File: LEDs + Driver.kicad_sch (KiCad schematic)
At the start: 1 part, among them U1 LP5860

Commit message: Progress commit. Added MCU + IMU.
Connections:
- net Bottom LEDs/SW5: now reaches U1.15 (SW5)
- net Bottom LEDs/SW6: now reaches U1.17 (SW6)
- net Bottom LEDs/SW7: now reaches U1.18 (SW7)
- net Bottom LEDs/SW8: now reaches U1.19 (SW8)
- net Bottom LEDs/SW9: now reaches U1.20 (SW9)
- net GND: now reaches U1.31 (AGND)
- net GND: now also U1.41 (GND)
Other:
- sheet Bottom LEDs ports: added SW5, SW6, SW7, SW8, SW9; removed none

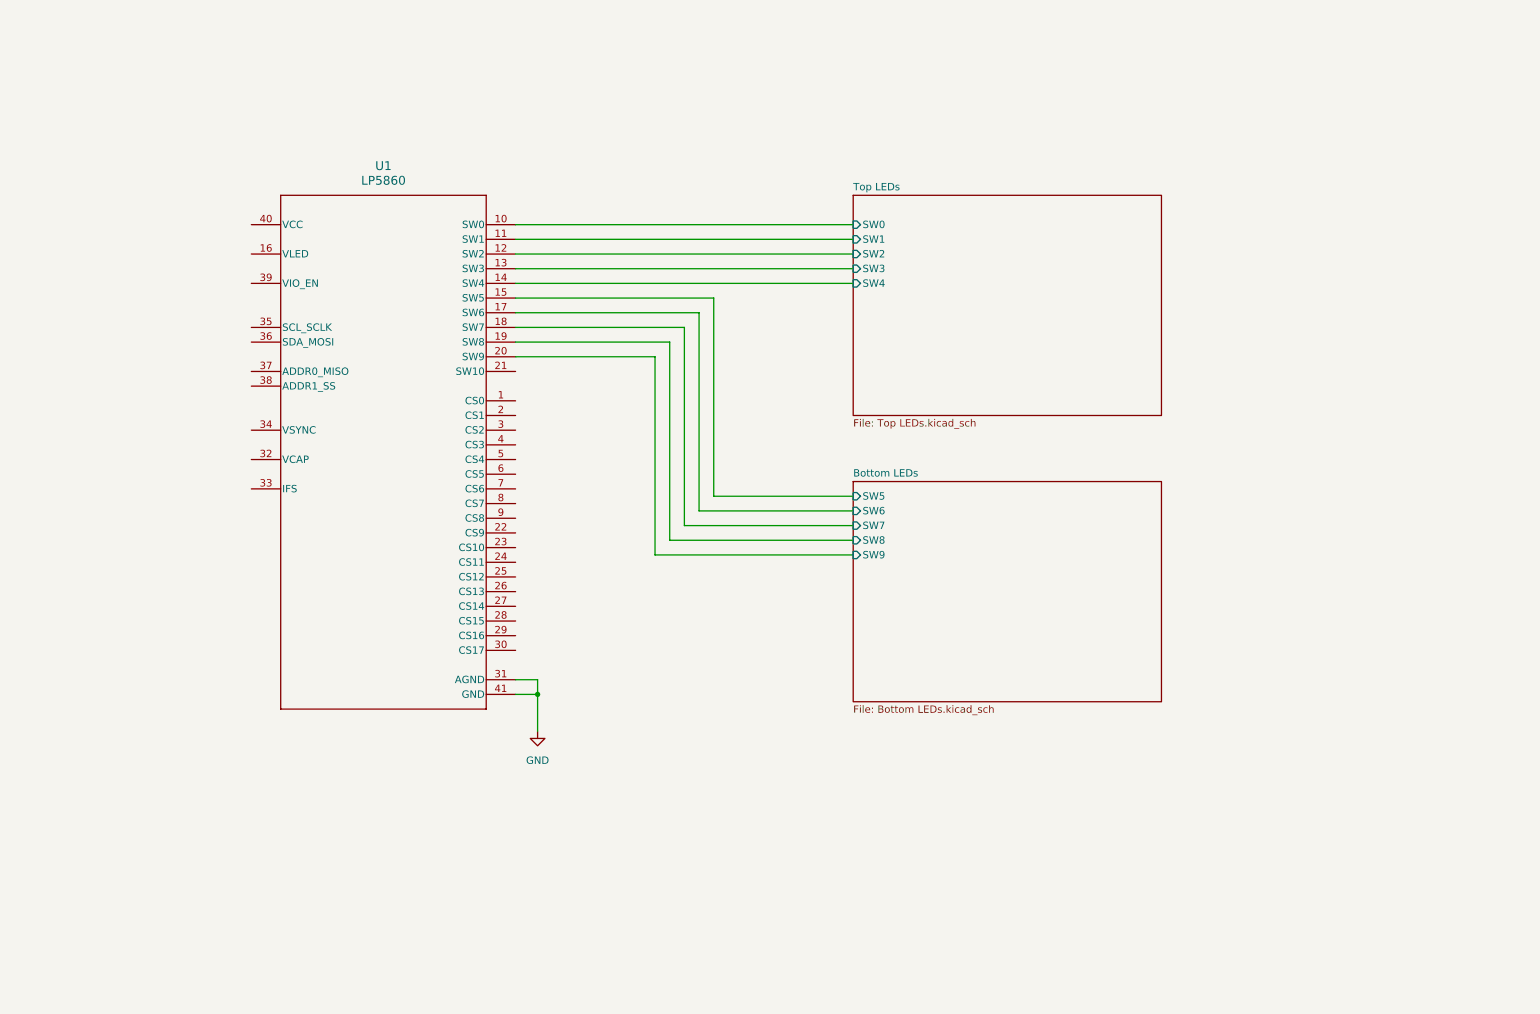
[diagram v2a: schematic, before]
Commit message: Initial complete implementation of LEDS.
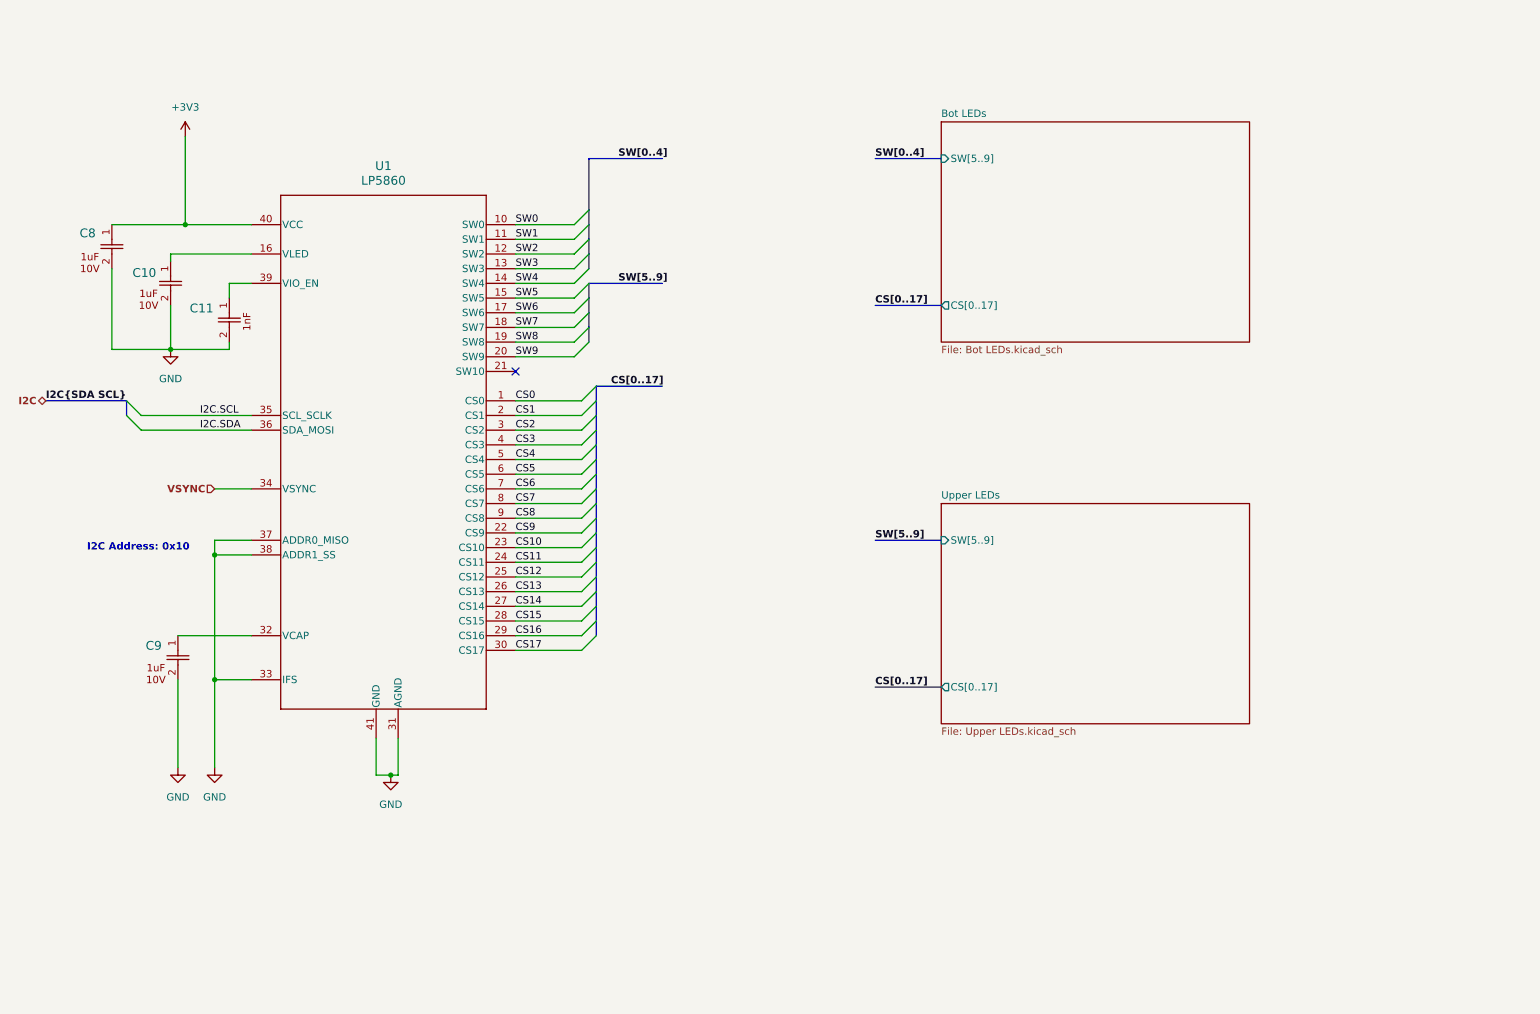
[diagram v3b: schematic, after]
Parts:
- added C10, C8, C9: GRM155Z71A105KE01D, Hourglass_footprint_library:CAP_GRM155Z_MUR, symbol Hourglass_symbol_library:GRM155Z71A105KE01D
- added C11: SH05B102K251DC, Hourglass_footprint_library:CAP_CL21_SAM, symbol Hourglass_symbol_library:SH05B102K251DC
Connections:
- net GND: now also U1.33 (IFS), U1.37 (ADDR0_MISO), U1.38 (ADDR1_SS), C10.2, C11.2, C8.2, C9.2
- net CS0: now reaches U1.1 (CS0)
- net at U1.16 (VLED): now also C10.1
- net CS1: now reaches U1.2 (CS1)
- net CS9: now reaches U1.22 (CS9)
- net CS10: now reaches U1.23 (CS10)
- net CS11: now reaches U1.24 (CS11)
- net CS12: now reaches U1.25 (CS12)
- net CS13: now reaches U1.26 (CS13)
- net CS14: now reaches U1.27 (CS14)
- net CS15: now reaches U1.28 (CS15)
- net CS16: now reaches U1.29 (CS16)
- net CS2: now reaches U1.3 (CS2)
- net CS17: now reaches U1.30 (CS17)
- net at U1.32 (VCAP): now also C9.1
- net VSYNC: now reaches U1.34 (VSYNC)
- net I2C.SCL: now reaches U1.35 (SCL_SCLK)
- net I2C.SDA: now reaches U1.36 (SDA_MOSI)
- net at U1.39 (VIO_EN): now also C11.1
- net CS3: now reaches U1.4 (CS3)
- net +3V3: now reaches U1.40 (VCC)
- net +3V3: now also C8.1
- net CS4: now reaches U1.5 (CS4)
- net CS5: now reaches U1.6 (CS5)
- net CS6: now reaches U1.7 (CS6)
- net CS7: now reaches U1.8 (CS7)
- net CS8: now reaches U1.9 (CS8)
- net Bottom LEDs/SW5 renamed SW5
- net Bottom LEDs/SW6 renamed SW6
- net Bottom LEDs/SW7 renamed SW7
- net Bottom LEDs/SW8 renamed SW8
- net Bottom LEDs/SW9 renamed SW9
- net Bot LEDs/SW0 renamed SW0
- net Bot LEDs/SW1 renamed SW1
- net Bot LEDs/SW2 renamed SW2
- net Bot LEDs/SW3 renamed SW3
- net Bot LEDs/SW4 renamed SW4
- no-connect marks 0 -> 1
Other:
- sheet Top LEDs renamed Bot LEDs
- removed sheet Bottom LEDs
- added sheet Upper LEDs (Upper LEDs.kicad_sch)
- sheet Bot LEDs: file Top LEDs.kicad_sch -> Bot LEDs.kicad_sch
- sheet Bot LEDs ports: added CS[0..17], SW[5..9]; removed SW0, SW1, SW2, SW3, SW4
- note added: "I2C Address: 0x10"
- moved on the sheet: U1

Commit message: Completed schematic for MCU section
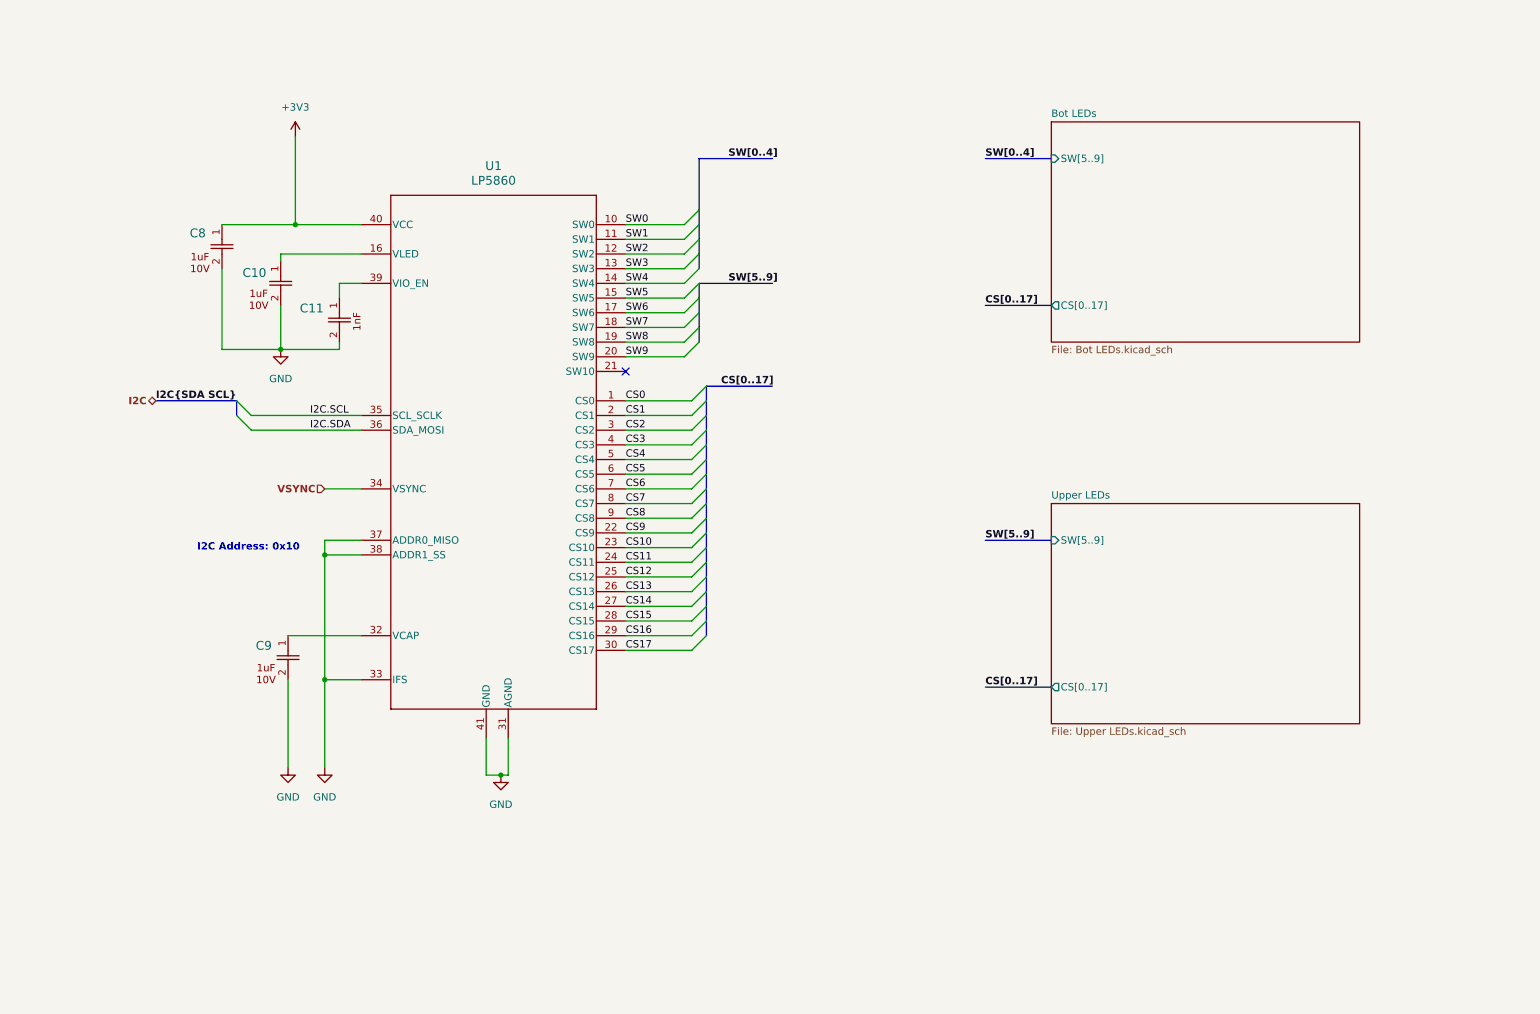
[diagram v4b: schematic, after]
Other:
- moved on the sheet: C10, C11, C8, C9, U1

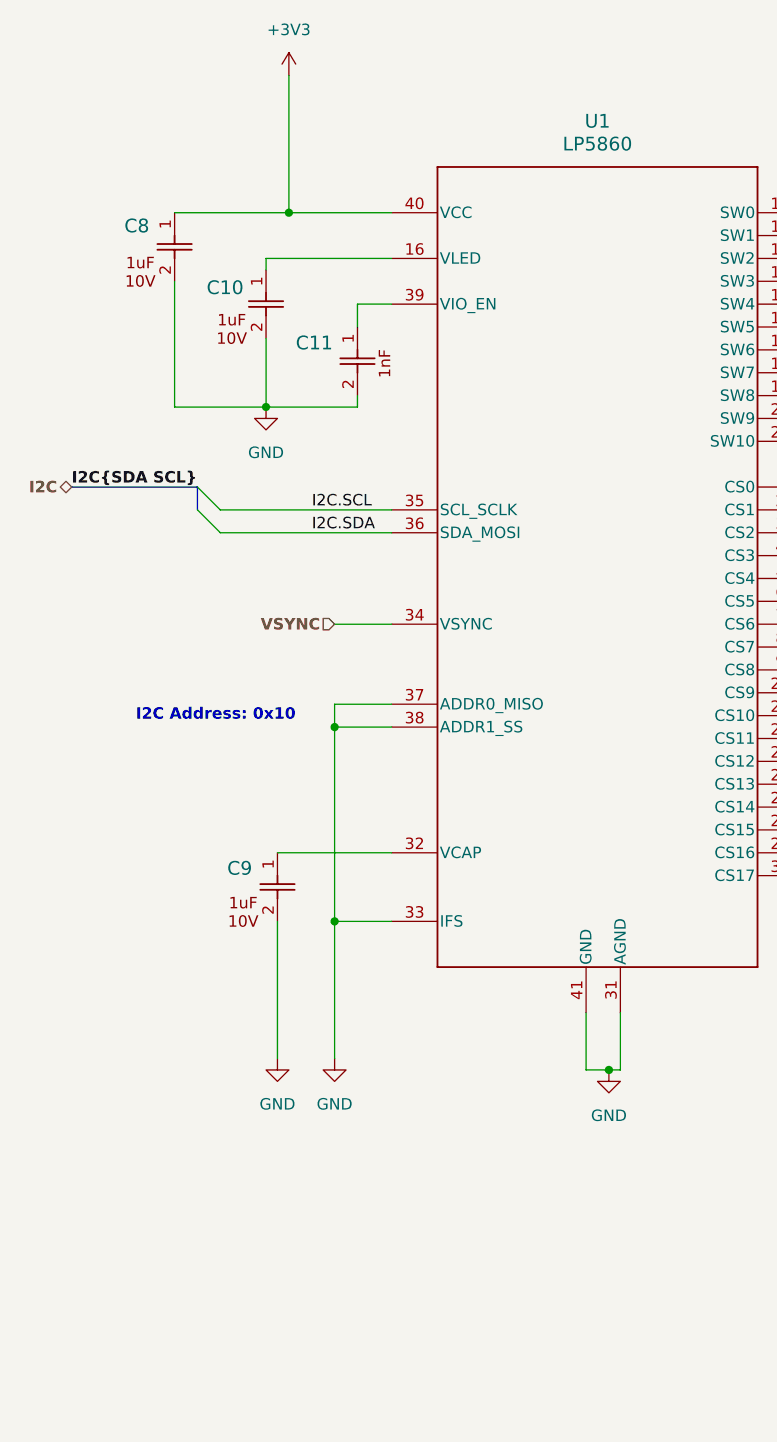
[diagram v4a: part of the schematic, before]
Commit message: First complete schematic with TPs.
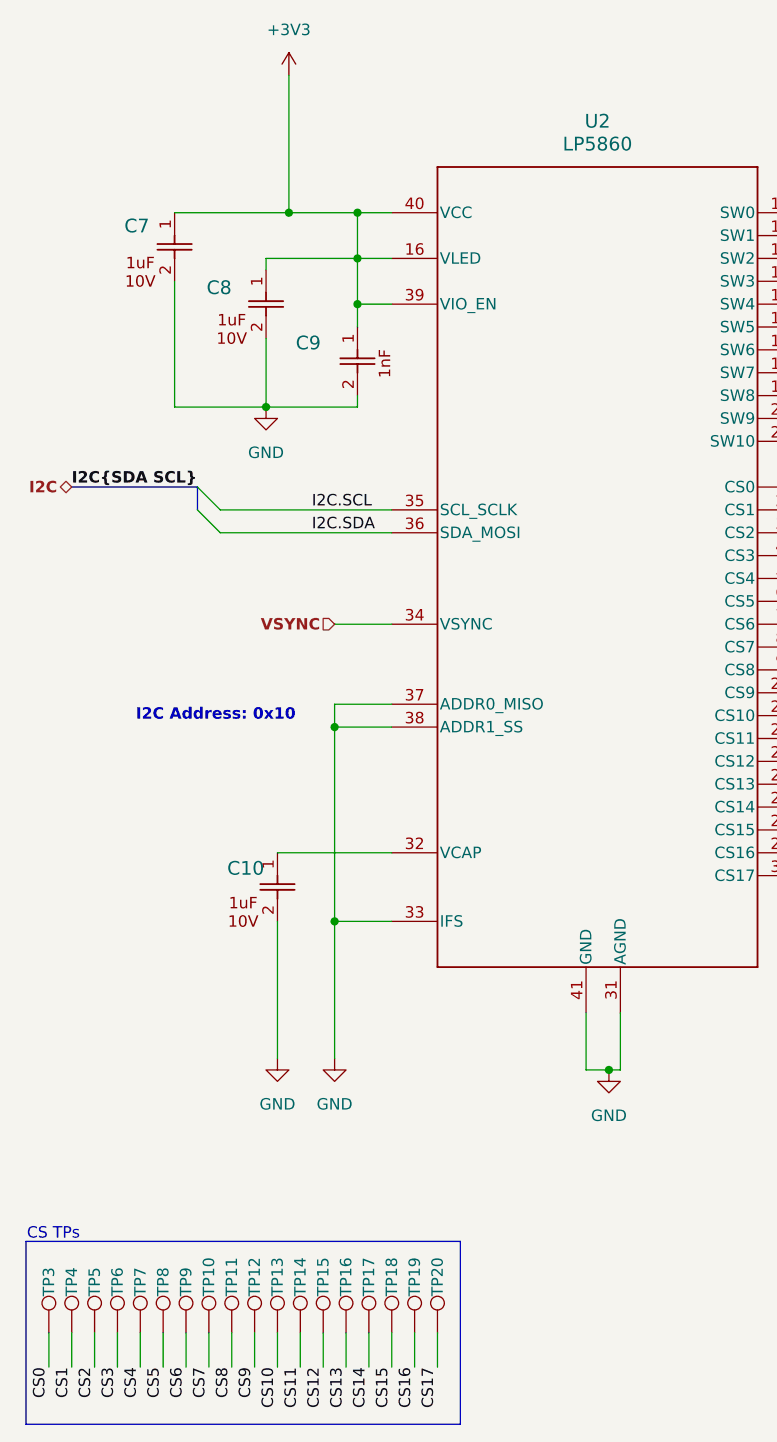
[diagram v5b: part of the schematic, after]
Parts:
- added TP10, TP11, TP12, TP13, TP14, TP15, TP16, TP17, TP18, TP19, TP20, TP3, TP4, TP5, TP6, TP7, TP8, TP9: TestPoint, TestPoint:TestPoint_Pad_D1.0mm, symbol Connector:TestPoint
- renumbered C9 to C10, C8 to C7, C10 to C8, C11 to C9, U1 to U2
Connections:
- net +3V3: now also C8.1, C9.1, U2.16 (VLED), U2.39 (VIO_EN)
- net CS0: now also TP3.1
- net CS1: now also TP4.1
- net CS10: now also TP13.1
- net CS11: now also TP14.1
- net CS12: now also TP15.1
- net CS13: now also TP16.1
- net CS14: now also TP17.1
- net CS15: now also TP18.1
- net CS16: now also TP19.1
- net CS17: now also TP20.1
- net CS2: now also TP5.1
- net CS3: now also TP6.1
- net CS4: now also TP7.1
- net CS5: now also TP8.1
- net CS6: now also TP9.1
- net CS7: now also TP10.1
- net CS8: now also TP11.1
- net CS9: now also TP12.1
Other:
- note added: "CS TPs"

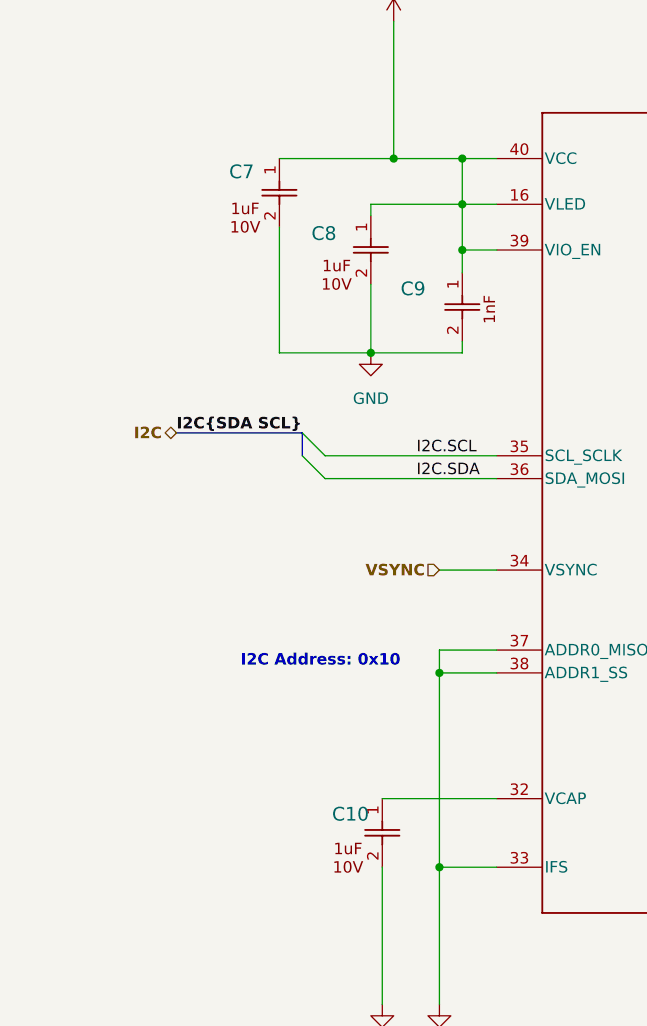
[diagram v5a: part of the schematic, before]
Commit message: Addressed DRC warnings and errors.
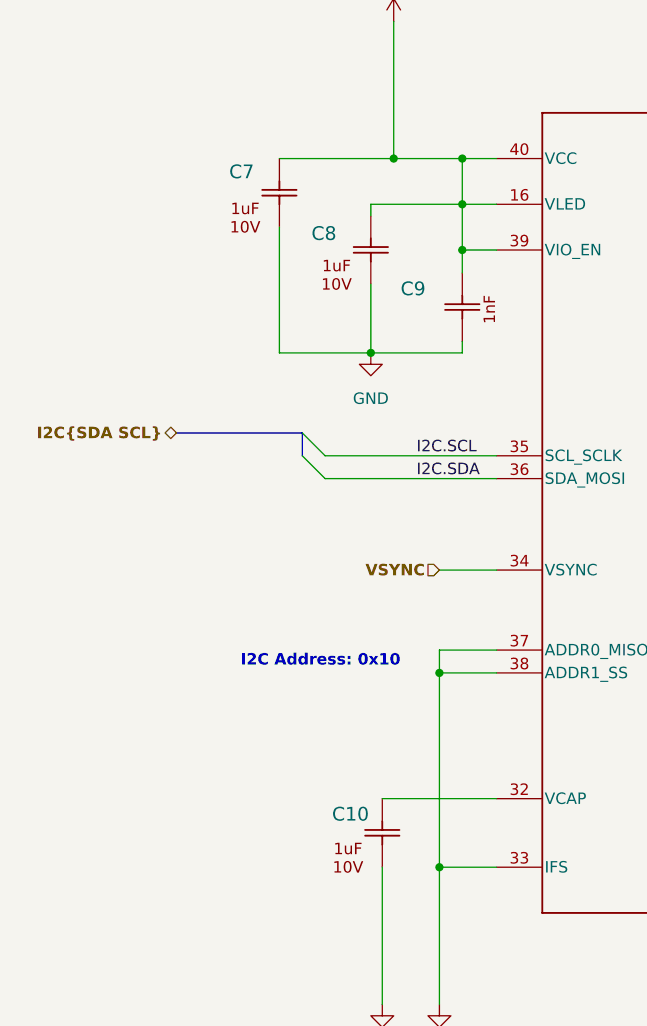
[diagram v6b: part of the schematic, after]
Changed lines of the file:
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@@
-		)
-	)
-	(label "I2C{SDA SCL}"
-		(at 40.64 83.82 0)
-		(effects
-			(font
-				(size 1.27 1.27)
-				(thickness 0.254)
-				(bold yes)
-			)
-			(justify left bottom)
 		)
 	)
@@
 		)
 	)
-	(hierarchical_label "I2C"
+	(hierarchical_label "I2C{SDA SCL}"
 		(shape bidirectional)
 		(at 40.64 83.82 180)
@@
 		(dnp no)
 		(fields_autoplaced yes)
-		(property "Reference" "#PWR015"
+		(property "Reference" "#PWR15"
 			(at 100.33 154.94 0)
 			(effects
@@
 			(project ""
 				(path "/a75630d2-15a7-42bc-8ce0-7846cbd1da6b/9c708963-e8cc-42a5-9c83-1e957695e1ca"
-					(reference "#PWR015")
+					(reference "#PWR15")
 					(unit 1)
 				)
@@
 		(dnp no)
 		(fields_autoplaced yes)
-		(property "Reference" "#PWR013"
+		(property "Reference" "#PWR13"
 			(at 63.5 153.67 0)
 			(effects
@@
 			(project "Hourglass_PCBA"
 				(path "/a75630d2-15a7-42bc-8ce0-7846cbd1da6b/9c708963-e8cc-42a5-9c83-1e957695e1ca"
-					(reference "#PWR013")
+					(reference "#PWR13")
 					(unit 1)
 				)
@@
 		(on_board yes)
 		(dnp no)
-		(property "Reference" "#PWR011"
+		(property "Reference" "#PWR11"
 			(at 64.77 41.91 0)
 			(effects
@@
 			(project ""
 				(path "/a75630d2-15a7-42bc-8ce0-7846cbd1da6b/9c708963-e8cc-42a5-9c83-1e957695e1ca"
-					(reference "#PWR011")
+					(reference "#PWR11")
 					(unit 1)
 				)
@@
 		(dnp no)
 		(fields_autoplaced yes)
-		(property "Reference" "#PWR012"
+		(property "Reference" "#PWR12"
 			(at 62.23 81.28 0)
 			(effects
@@
 			(project ""
 				(path "/a75630d2-15a7-42bc-8ce0-7846cbd1da6b/9c708963-e8cc-42a5-9c83-1e957695e1ca"
-					(reference "#PWR012")
+					(reference "#PWR12")
 					(unit 1)
 				)
@@
 		(dnp no)
 		(fields_autoplaced yes)
-		(property "Reference" "#PWR014"
+		(property "Reference" "#PWR14"
 			(at 69.85 153.67 0)
 			(effects
@@
 			(project "Hourglass_PCBA"
 				(path "/a75630d2-15a7-42bc-8ce0-7846cbd1da6b/9c708963-e8cc-42a5-9c83-1e957695e1ca"
-					(reference "#PWR014")
-					(unit 1)
-				)
+					(reference "#PWR14")
+					(unit 1)
+				)

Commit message: Added comments on schematic and fixed bus for SW[0..4] on Bot LEDs.
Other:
- sheet Bot LEDs ports: added SW[0..4]; removed SW[5..9]
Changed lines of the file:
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@@
 			)
 		)
-		(pin "SW[5..9]" input
+		(pin "SW[0..4]" input
 			(at 195.58 41.91 180)
 			(effects
